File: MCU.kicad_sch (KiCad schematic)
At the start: 30 parts, among them J3 GPIO, J5 Debugger Pins

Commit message: Add proper footprints
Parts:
- C? (x14): footprint Capacitor_SMD:C_0402_1005Metric -> Capacitor_SMD:C_0603_1608Metric
- C? (x3): footprint Capacitor_SMD:C_0805_2012Metric -> Capacitor_SMD:C_0603_1608Metric
- J5: footprint (none) -> Connector_JST:JST_XH_B4B-XH-AM_1x04_P2.50mm_Vertical
- J?: footprint RP2040_minimal:USB_Micro-B_Amphenol_10103594-0001LF_Horizontal_modified -> Connector_USB:USB_Micro-B_Molex-105017-0001
- R?: footprint Capacitor_SMD:C_0402_1005Metric -> (none)
- R? (x4): footprint Capacitor_SMD:C_0402_1005Metric -> Resistor_SMD:R_0603_1608Metric
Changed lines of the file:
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@@
       (effects (font (size 1.27 1.27)) (justify left))
     )
-    (property "Footprint" "Capacitor_SMD:C_0402_1005Metric" (at 55.372 87.63 90)
+    (property "Footprint" "" (at 55.372 87.63 90)
       (effects (font (size 1.27 1.27)) hide)
     )
@@
       (effects (font (size 1.27 1.27)))
     )
-    (property "Footprint" "Capacitor_SMD:C_0402_1005Metric" (at 212.09 66.802 90)
+    (property "Footprint" "Resistor_SMD:R_0603_1608Metric" (at 212.09 66.802 90)
       (effects (font (size 1.27 1.27)) hide)
     )
@@
       (effects (font (size 1.27 1.27)) (justify left))
     )
-    (property "Footprint" "Capacitor_SMD:C_0402_1005Metric" (at 225.7552 36.83 0)
+    (property "Footprint" "Capacitor_SMD:C_0603_1608Metric" (at 225.7552 36.83 0)
       (effects (font (size 1.27 1.27)) hide)
     )
@@
       (effects (font (size 1.27 1.27)) (justify left))
     )
-    (property "Footprint" "Capacitor_SMD:C_0402_1005Metric" (at 40.64 135.5852 0)
+    (property "Footprint" "Capacitor_SMD:C_0603_1608Metric" (at 40.64 135.5852 0)
       (effects (font (size 1.27 1.27)) hide)
     )
@@
       (effects (font (size 1.27 1.27)) (justify left))
     )
-    (property "Footprint" "Capacitor_SMD:C_0402_1005Metric" (at 237.1852 36.83 0)
+    (property "Footprint" "Capacitor_SMD:C_0603_1608Metric" (at 237.1852 36.83 0)
       (effects (font (size 1.27 1.27)) hide)
     )
@@
       (effects (font (size 1.27 1.27)) (justify left))
     )
-    (property "Footprint" "Capacitor_SMD:C_0805_2012Metric" (at 275.2852 39.37 0)
+    (property "Footprint" "Capacitor_SMD:C_0603_1608Metric" (at 275.2852 39.37 0)
       (effects (font (size 1.27 1.27)) hide)
     )
@@
       (effects (font (size 1.27 1.27)) (justify left))
     )
-    (property "Footprint" "Capacitor_SMD:C_0402_1005Metric" (at 40.64 145.7452 0)
+    (property "Footprint" "Capacitor_SMD:C_0603_1608Metric" (at 40.64 145.7452 0)
       (effects (font (size 1.27 1.27)) hide)
     )
@@
       (effects (font (size 1.27 1.27)) (justify left))
     )
-    (property "Footprint" "Capacitor_SMD:C_0402_1005Metric" (at 136.8552 36.83 0)
+    (property "Footprint" "Capacitor_SMD:C_0603_1608Metric" (at 136.8552 36.83 0)
       (effects (font (size 1.27 1.27)) hide)
     )
@@
       (effects (font (size 1.27 1.27)) (justify left))
     )
-    (property "Footprint" "Capacitor_SMD:C_0402_1005Metric" (at 260.0452 36.83 0)
+    (property "Footprint" "Capacitor_SMD:C_0603_1608Metric" (at 260.0452 36.83 0)
       (effects (font (size 1.27 1.27)) hide)
     )
@@
       (effects (font (size 1.27 1.27)) (justify left))
     )
-    (property "Footprint" "Capacitor_SMD:C_0402_1005Metric" (at 214.3252 36.83 0)
+    (property "Footprint" "Capacitor_SMD:C_0603_1608Metric" (at 214.3252 36.83 0)
       (effects (font (size 1.27 1.27)) hide)
     )
@@
       (effects (font (size 1.27 1.27)))
     )
-    (property "Footprint" "Capacitor_SMD:C_0402_1005Metric" (at 41.91 101.092 90)
+    (property "Footprint" "Resistor_SMD:R_0603_1608Metric" (at 41.91 101.092 90)
       (effects (font (size 1.27 1.27)) hide)
     )
@@
       (effects (font (size 1.27 1.27)) (justify right))
     )
-    (property "Footprint" "RP2040_minimal:USB_Micro-B_Amphenol_10103594-0001LF_Horizontal_modified" (at 35.56 40.64 0)
+    (property "Footprint" "Connector_USB:USB_Micro-B_Molex-105017-0001" (at 35.56 40.64 0)
       (effects (font (size 1.27 1.27)) hide)
     )
@@
       (effects (font (size 1.27 1.27)))
     )
-    (property "Footprint" "Capacitor_SMD:C_0402_1005Metric" (at 212.09 69.342 90)
+    (property "Footprint" "Resistor_SMD:R_0603_1608Metric" (at 212.09 69.342 90)
       (effects (font (size 1.27 1.27)) hide)
     )
@@
       (effects (font (size 1.27 1.27)) (justify left))
     )
-    (property "Footprint" "Capacitor_SMD:C_0402_1005Metric" (at 248.6152 36.83 0)
+    (property "Footprint" "Capacitor_SMD:C_0603_1608Metric" (at 248.6152 36.83 0)
       (effects (font (size 1.27 1.27)) hide)
     )
@@
       (effects (font (size 1.27 1.27)) (justify left))
     )
-    (property "Footprint" "Capacitor_SMD:C_0805_2012Metric" (at 93.6752 43.18 0)
+    (property "Footprint" "Capacitor_SMD:C_0603_1608Metric" (at 93.6752 43.18 0)
       (effects (font (size 1.27 1.27)) hide)
     )
@@
       (effects (font (size 1.27 1.27)) (justify left))
     )
-    (property "Footprint" "Capacitor_SMD:C_0402_1005Metric" (at 79.7052 87.63 0)
+    (property "Footprint" "Capacitor_SMD:C_0603_1608Metric" (at 79.7052 87.63 0)
       (effects (font (size 1.27 1.27)) hide)
     )
@@
       (effects (font (size 1.27 1.27)) (justify left))
     )
-    (property "Footprint" "Capacitor_SMD:C_0805_2012Metric" (at 58.1152 43.18 0)
+    (property "Footprint" "Capacitor_SMD:C_0603_1608Metric" (at 58.1152 43.18 0)
       (effects (font (size 1.27 1.27)) hide)
     )
@@
       (effects (font (size 1.27 1.27)) (justify left))
     )
-    (property "Footprint" "Capacitor_SMD:C_0402_1005Metric" (at 191.4652 36.83 0)
+    (property "Footprint" "Capacitor_SMD:C_0603_1608Metric" (at 191.4652 36.83 0)
       (effects (font (size 1.27 1.27)) hide)
     )
@@
       (effects (font (size 1.27 1.27)) (justify left))
     )
-    (property "Footprint" "Capacitor_SMD:C_0402_1005Metric" (at 125.4252 36.83 0)
+    (property "Footprint" "Capacitor_SMD:C_0603_1608Metric" (at 125.4252 36.83 0)
       (effects (font (size 1.27 1.27)) hide)
     )
@@
       (effects (font (size 1.27 1.27)) (justify left))
     )
-    (property "Footprint" "Capacitor_SMD:C_0402_1005Metric" (at 202.8952 36.83 0)
+    (property "Footprint" "Capacitor_SMD:C_0603_1608Metric" (at 202.8952 36.83 0)
       (effects (font (size 1.27 1.27)) hide)
     )
@@
       (effects (font (size 1.27 1.27)))
     )
-    (property "Footprint" "" (at 43.18 176.53 0)
+    (property "Footprint" "Connector_JST:JST_XH_B4B-XH-AM_1x04_P2.50mm_Vertical" (at 43.18 176.53 0)
       (effects (font (size 1.27 1.27)) hide)
     )
@@
       (effects (font (size 1.27 1.27)))
     )
-    (property "Footprint" "Capacitor_SMD:C_0402_1005Metric" (at 68.58 143.002 90)
+    (property "Footprint" "Resistor_SMD:R_0603_1608Metric" (at 68.58 143.002 90)
       (effects (font (size 1.27 1.27)) hide)
     )
@@
       (effects (font (size 1.27 1.27)) (justify left))
     )
-    (property "Footprint" "Capacitor_SMD:C_0402_1005Metric" (at 136.8552 52.07 0)
+    (property "Footprint" "Capacitor_SMD:C_0603_1608Metric" (at 136.8552 52.07 0)
       (effects (font (size 1.27 1.27)) hide)
     )
@@
       (effects (font (size 1.27 1.27)) (justify left))
     )
-    (property "Footprint" "Capacitor_SMD:C_0402_1005Metric" (at 191.4652 52.07 0)
-      (effects (font (size 1.27 1.27)) hide)
-    )
+    (property "Footprint" "Capacitor_SMD:C_0603_1608Metric" (at 191.4652 52.07 0)
+      (effects (font (size 1.27 1.27)) hide)
+    )

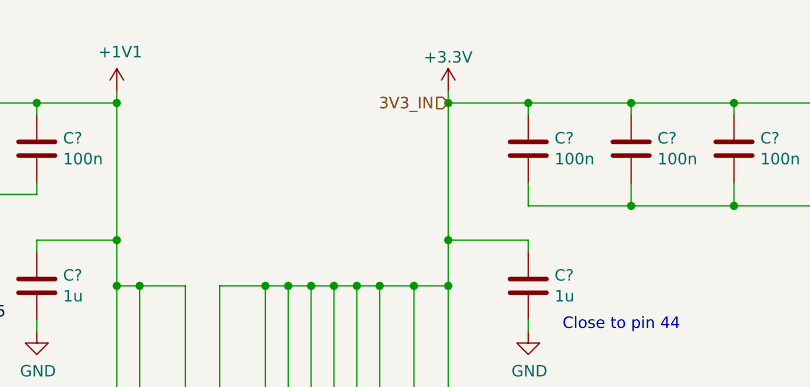
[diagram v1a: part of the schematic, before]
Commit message: Add proper JST Connector
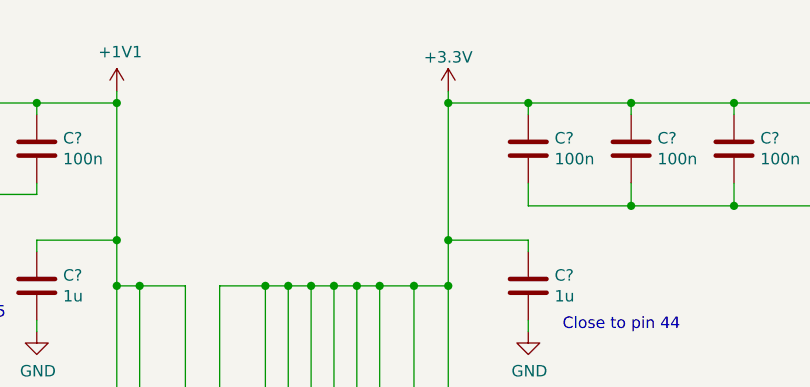
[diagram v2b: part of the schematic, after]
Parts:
- J5: footprint Connector_JST:JST_XH_B4B-XH-AM_1x04_P2.50mm_Vertical -> Connector_JST:JST_XH_B4B-XH-A_1x04_P2.50mm_Vertical
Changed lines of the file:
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@@
     (effects (font (size 1.27 1.27)) (justify left))
-  )
-  (hierarchical_label "3V3_IN" (shape input) (at 181.61 27.94 180) (fields_autoplaced)
-    (effects (font (size 1.27 1.27)) (justify right))
   )
   (hierarchical_label "OUT_H2" (shape output) (at 212.09 127 0) (fields_autoplaced)
@@
       (effects (font (size 1.27 1.27)))
     )
-    (property "Footprint" "Connector_JST:JST_XH_B4B-XH-AM_1x04_P2.50mm_Vertical" (at 43.18 176.53 0)
-      (effects (font (size 1.27 1.27)) hide)
-    )
+    (property "Footprint" "Connector_JST:JST_XH_B4B-XH-A_1x04_P2.50mm_Vertical" (at 43.18 176.53 0)
+      (effects (font (size 1.27 1.27)) hide)
+    )

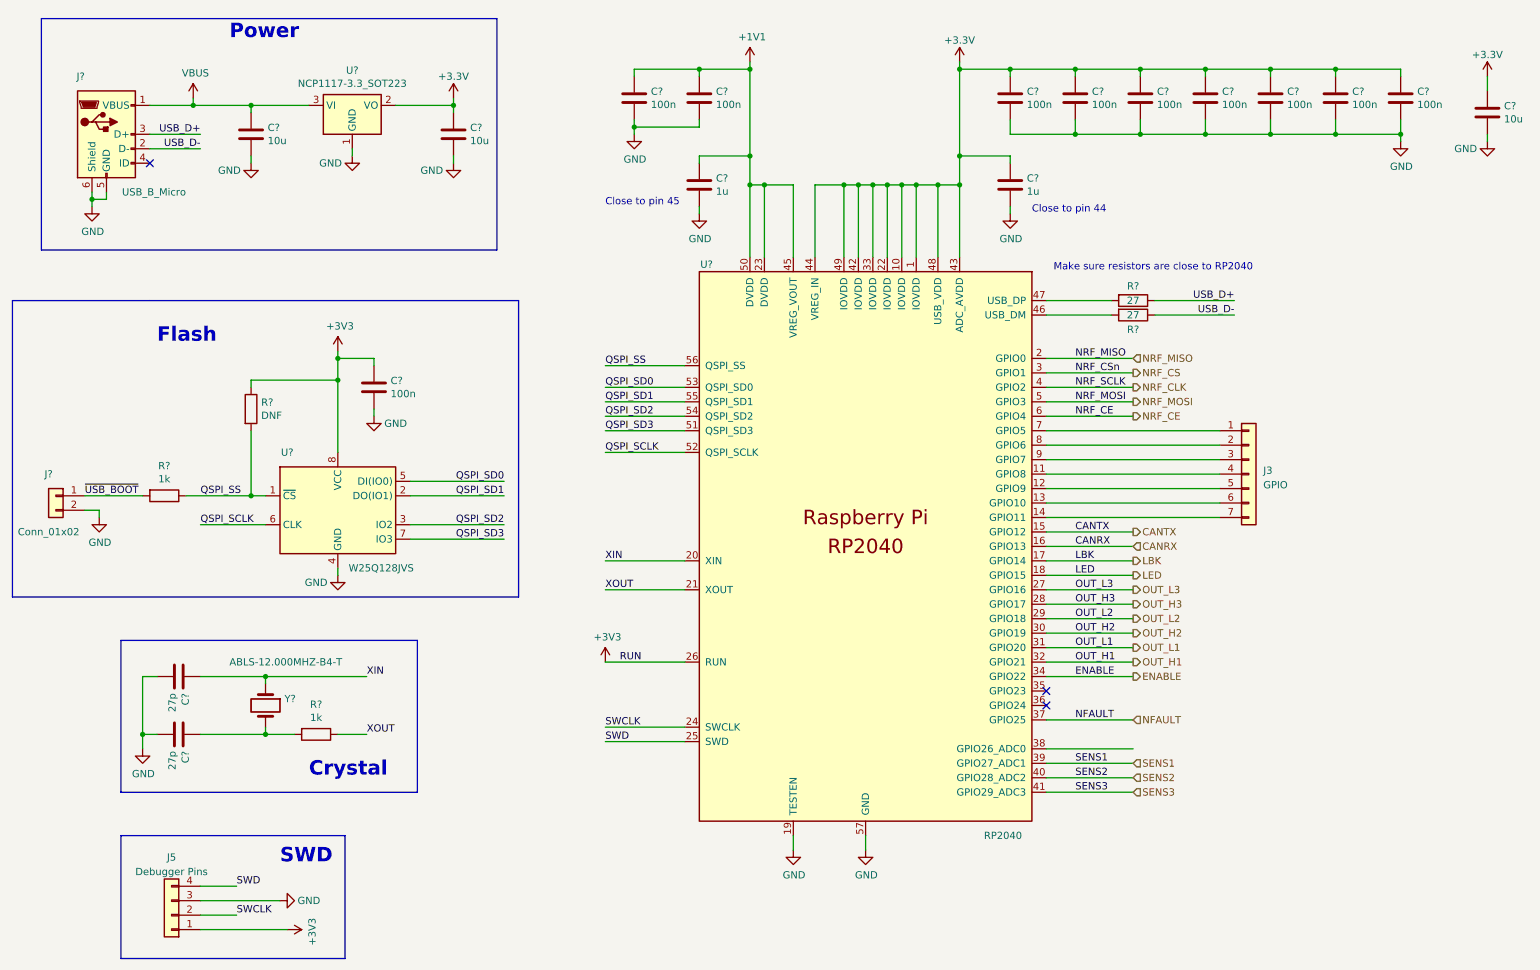
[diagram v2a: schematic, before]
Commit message: fix ERC
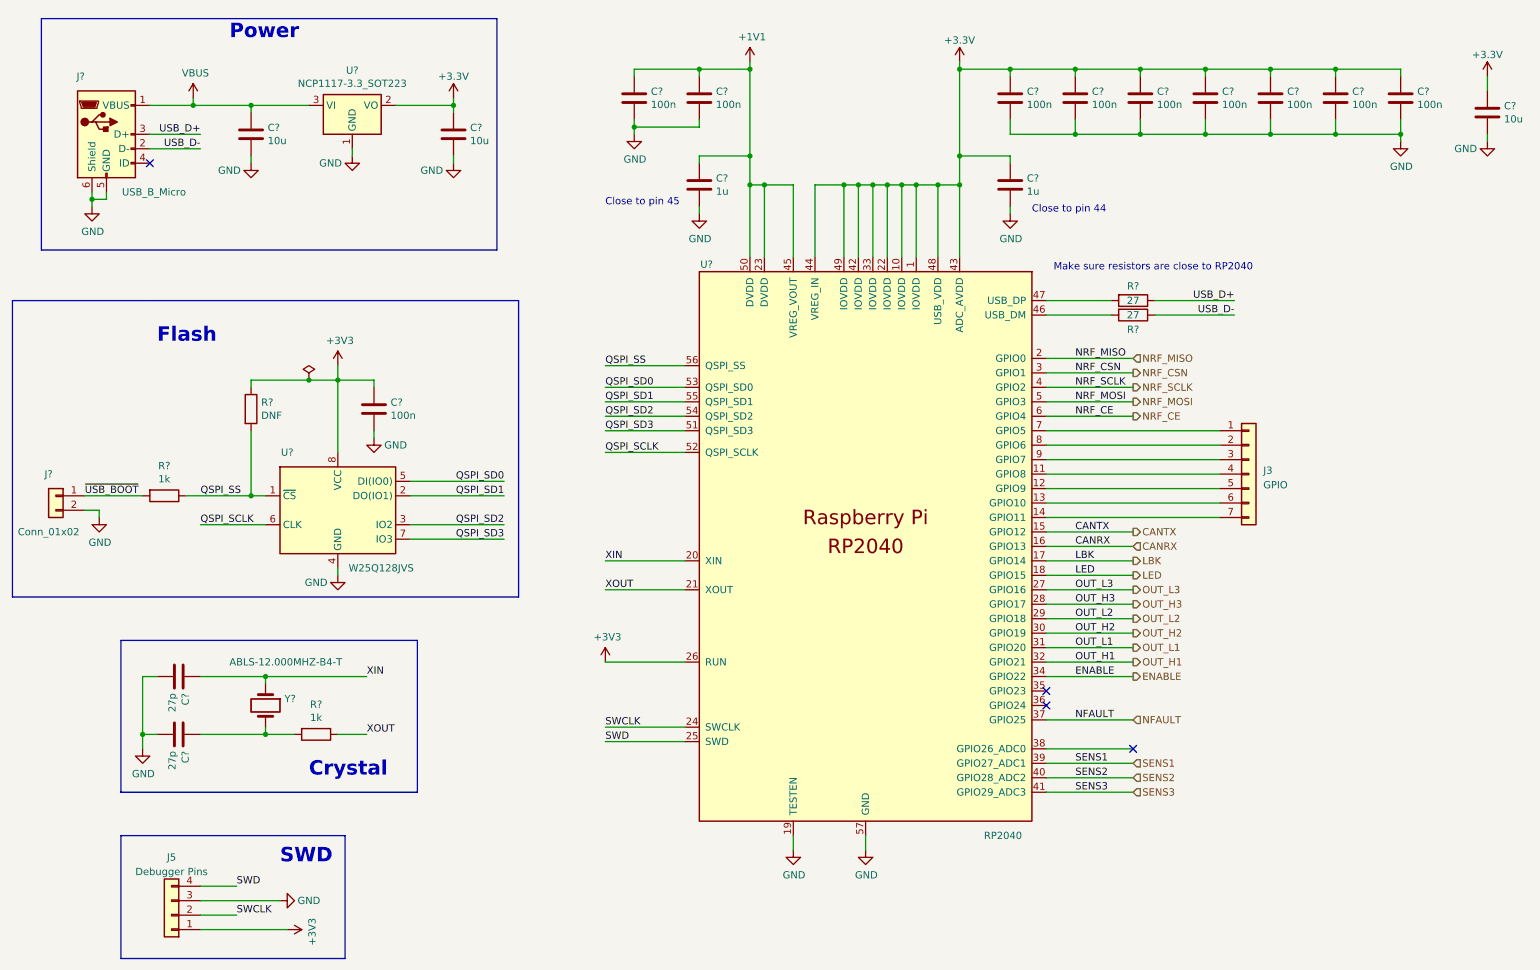
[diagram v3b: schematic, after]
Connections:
- net NRF_CLK renamed NRF_SCLK
- net NRF_CS renamed NRF_CSN
- no-connect marks 3 -> 4
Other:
- moved on the sheet: C?

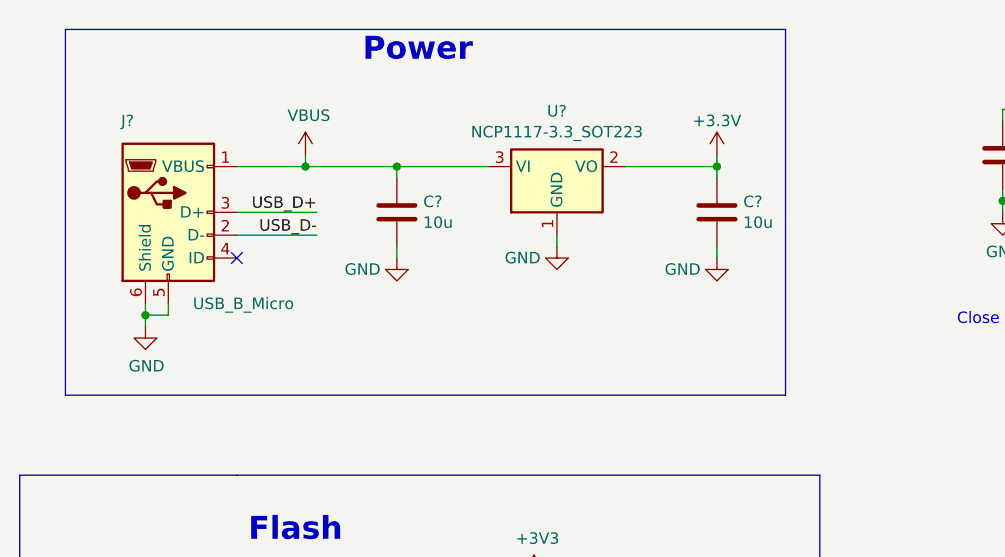
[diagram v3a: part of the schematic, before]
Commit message: fixed ERC violations
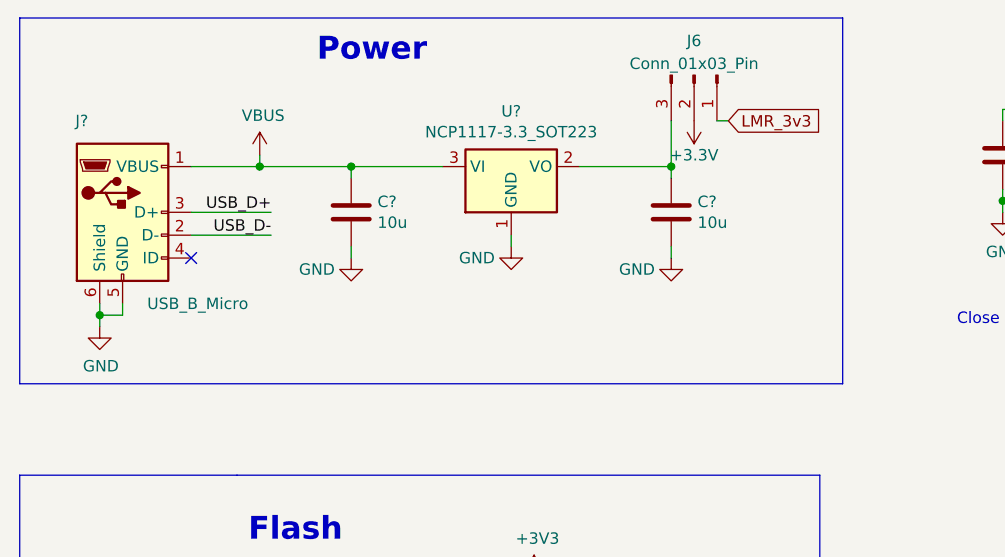
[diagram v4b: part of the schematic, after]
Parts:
- added J6: Conn_01x03_Pin, Connector_PinHeader_2.54mm:PinHeader_1x03_P2.54mm_Vertical, symbol Connector:Conn_01x03_Pin
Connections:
- net +3.3V: now also J6.2 (Pin_2); no longer C?.1, U?.2 (VO)
- new net: C?.1, J6.3 (Pin_3), U?.2 (VO)
- new net LMR_3v3: J6.1 (Pin_1)
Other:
- moved on the sheet: C?, J?, U?

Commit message: Final schematic with no DRC errors
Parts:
- removed J6: Conn_01x03_Pin, Connector_PinHeader_2.54mm:PinHeader_1x03_P2.54mm_Vertical, symbol Connector:Conn_01x03_Pin
- C?: footprint Capacitor_SMD:C_0603_1608Metric -> Capacitor_THT:CP_Radial_D5.0mm_P2.50mm
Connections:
- net +3V3 is gone; now on net +3.3V: C?.1, J5.1 (Pin_1), R?.1, U?.26 (RUN), U?.8 (VCC)
- net +3.3V: now also C?.1, U?.2 (VO)
